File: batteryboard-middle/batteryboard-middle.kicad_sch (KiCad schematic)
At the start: 10 parts, among them J1 Conn_01x02, J2 Conn_01x02, J3 FLE-110-01-G-DV-A, J4 FLE-110-01-G-DV-A, J5 FTS-110-01-L-DV-A, J6 FTS-110-01-L-DV-A

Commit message: Fixed Broken Merge
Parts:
- removed J3, J4: FLE-110-01-G-DV-A, mainboard:SAMTEC_FLE-110-01-G-DV-A, symbol Connector_Generic:Conn_02x10_Odd_Even
- removed J5, J6: FTS-110-01-L-DV-A, batteryboard:SAMTEC-FTS-110-01-X-DV-A, symbol Connector_Generic:Conn_02x10_Odd_Even
- added J1: FLE-105-01-G-DV-A, batteryboard:SAMTEC_FLE-105-01-G-DV-A, symbol Connector_Generic:Conn_02x05_Odd_Even
- added J4: FTS-105-01-L-DV-A, batteryboard:FTS-105-XX-YY-DV-A, symbol Connector_Generic:Conn_02x05_Odd_Even
- renumbered J1 to J3
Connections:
- net +3V3: now also J1.3 (Pin_3), J4.3 (Pin_3)
- net BATT_N_SW: now also J1.2 (Pin_2)
- net BATT_P: now also J1.9 (Pin_9), J4.9 (Pin_9)
- net BATT_P_SW: now also J1.1 (Pin_1)
- net GND: now also J1.4 (Pin_4), J4.4 (Pin_4)
- new net COIL_N: J1.8 (Pin_8), J4.8 (Pin_8)
- new net COIL_P: J1.7 (Pin_7), J4.7 (Pin_7)
- new net SCL3: J1.6 (Pin_6), J4.6 (Pin_6)
- new net SDA3: J1.5 (Pin_5), J4.5 (Pin_5)
- new net VBUS: J1.10 (Pin_10), J4.10 (Pin_10)
- no-connect marks 32 -> 2
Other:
- moved on the sheet: H1, H2, H3, H4, J2, J3

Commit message: Some changes
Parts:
- removed J1: FLE-105-01-G-DV-A, batteryboard:SAMTEC_FLE-105-01-G-DV-A, symbol Connector_Generic:Conn_02x05_Odd_Even
- removed J4: FTS-105-01-L-DV-A, batteryboard:FTS-105-XX-YY-DV-A, symbol Connector_Generic:Conn_02x05_Odd_Even
- added J1: FLE-107-01-G-DV-A, batteryboard:SAMTEC_FLE-107-01-G-DV-A, symbol Connector_Generic:Conn_02x07_Odd_Even
- added J4: FTS-107-01-L-DV-A, batteryboard:SAMTEC-FTS-107-01-X-DV-A, symbol Connector_Generic:Conn_02x07_Odd_Even
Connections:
- net +3V3: now also J1.3 (Pin_3), J1.5 (Pin_5), J4.3 (Pin_3), J4.5 (Pin_5)
- net BATT_N_SW: now also J1.10 (Pin_10), J1.8 (Pin_8), J4.10 (Pin_10), J4.8 (Pin_8)
- net BATT_P: now also J1.7 (Pin_7), J1.9 (Pin_9), J4.7 (Pin_7), J4.9 (Pin_9)
- net BATT_P_SW: now also J1.4 (Pin_4), J1.6 (Pin_6), J4.4 (Pin_4), J4.6 (Pin_6)
- net GND: now also J1.1 (Pin_1), J1.2 (Pin_2), J4.1 (Pin_1), J4.2 (Pin_2)
- new net COIL5_N: J1.14 (Pin_14), J4.14 (Pin_14)
- new net COIL5_P: J1.12 (Pin_12), J4.12 (Pin_12)
- new net SCL1: J1.11 (Pin_11), J4.11 (Pin_11)
- new net SDA1: J1.13 (Pin_13), J4.13 (Pin_13)
- no-connect marks 2 -> 0
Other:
- note added: "Stack Conn - From Bottom Batteryboard"
- note added: "Stack Conn - To Top Batteryboard"
- note removed: "Stack Conn - From Batteryboard Bottom"
- note removed: "Stack Conn - To Batteryboard Top"
- moved on the sheet: H1, H2, H3, H4

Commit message: B2/01 Updates
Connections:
- net +3V3: now also J1.7 (Pin_7), J4.7 (Pin_7); no longer J1.3 (Pin_3), J4.3 (Pin_3)
- net BATT_N_SW: now also J1.2 (Pin_2), J1.4 (Pin_4), J4.2 (Pin_2), J4.4 (Pin_4); no longer J1.10 (Pin_10), J1.8 (Pin_8), J4.10 (Pin_10), J4.8 (Pin_8)
- net BATT_P: now also J1.10 (Pin_10), J1.12 (Pin_12), J4.10 (Pin_10), J4.12 (Pin_12); no longer J1.7 (Pin_7), J1.9 (Pin_9), J4.7 (Pin_7), J4.9 (Pin_9)
- net BATT_P_SW: now also J1.8 (Pin_8), J4.8 (Pin_8); no longer J1.4 (Pin_4), J4.4 (Pin_4)
- net COIL5_P: now also J1.13 (Pin_13), J4.13 (Pin_13); no longer J1.12 (Pin_12), J4.12 (Pin_12)
- net GND: now also J1.3 (Pin_3), J4.3 (Pin_3); no longer J1.2 (Pin_2), J4.2 (Pin_2)
- net SCL1: now also J1.9 (Pin_9), J4.9 (Pin_9); no longer J1.11 (Pin_11), J4.11 (Pin_11)
- net SDA1: now also J1.11 (Pin_11), J4.11 (Pin_11); no longer J1.13 (Pin_13), J4.13 (Pin_13)
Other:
- moved on the sheet: J1

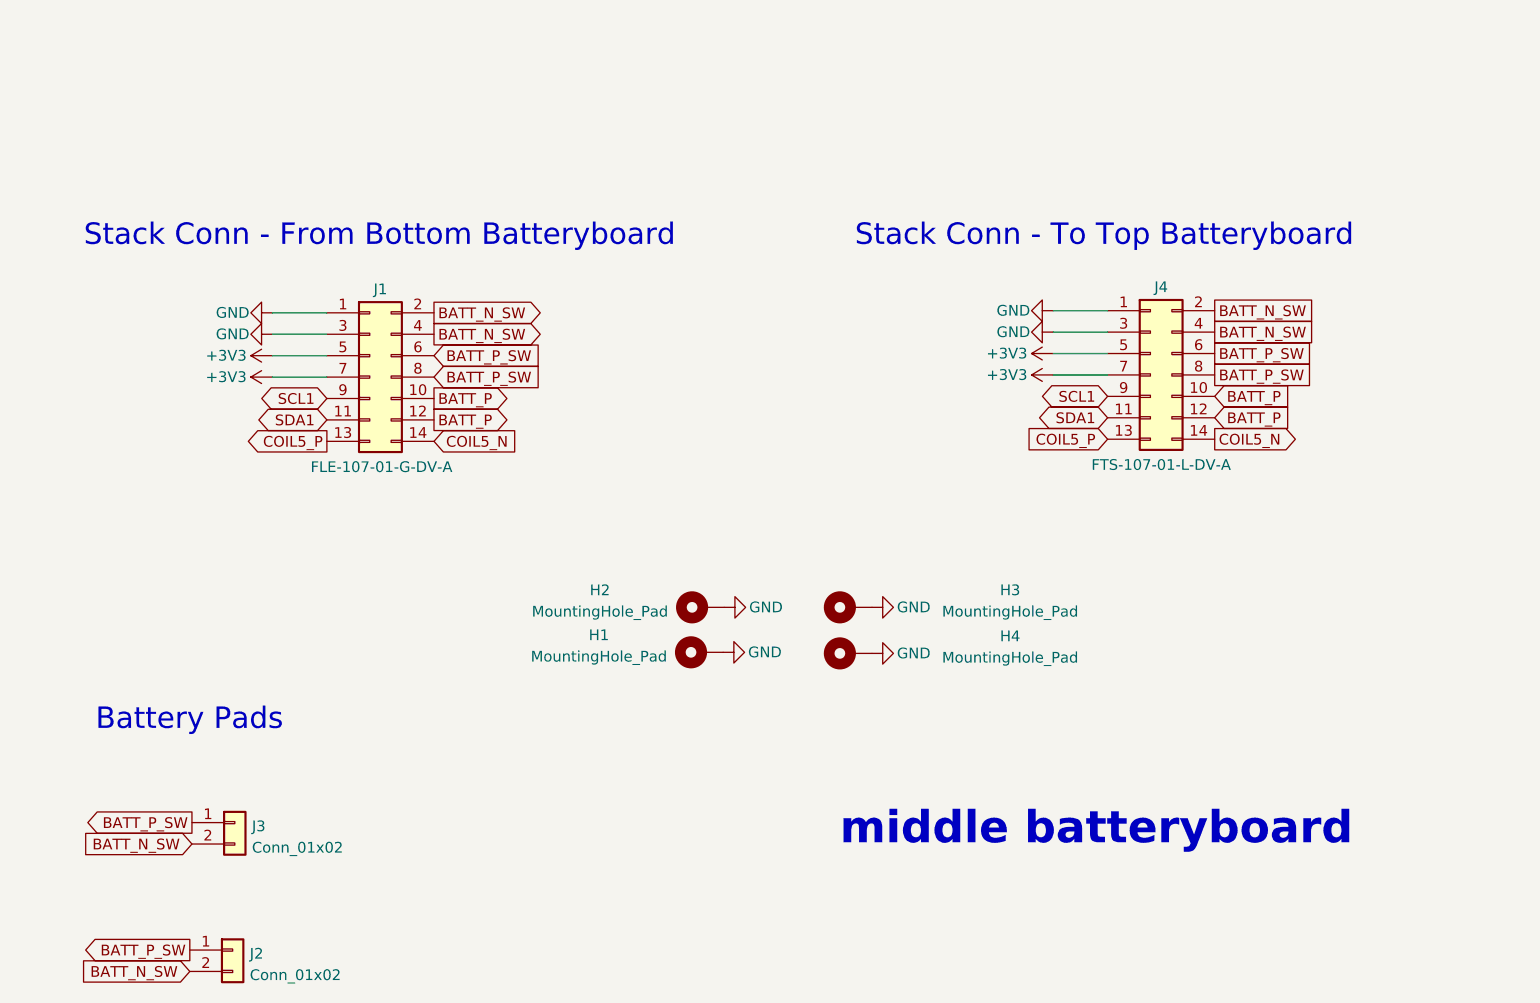
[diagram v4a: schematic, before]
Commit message: Updated batteryboards for Rev B3/01
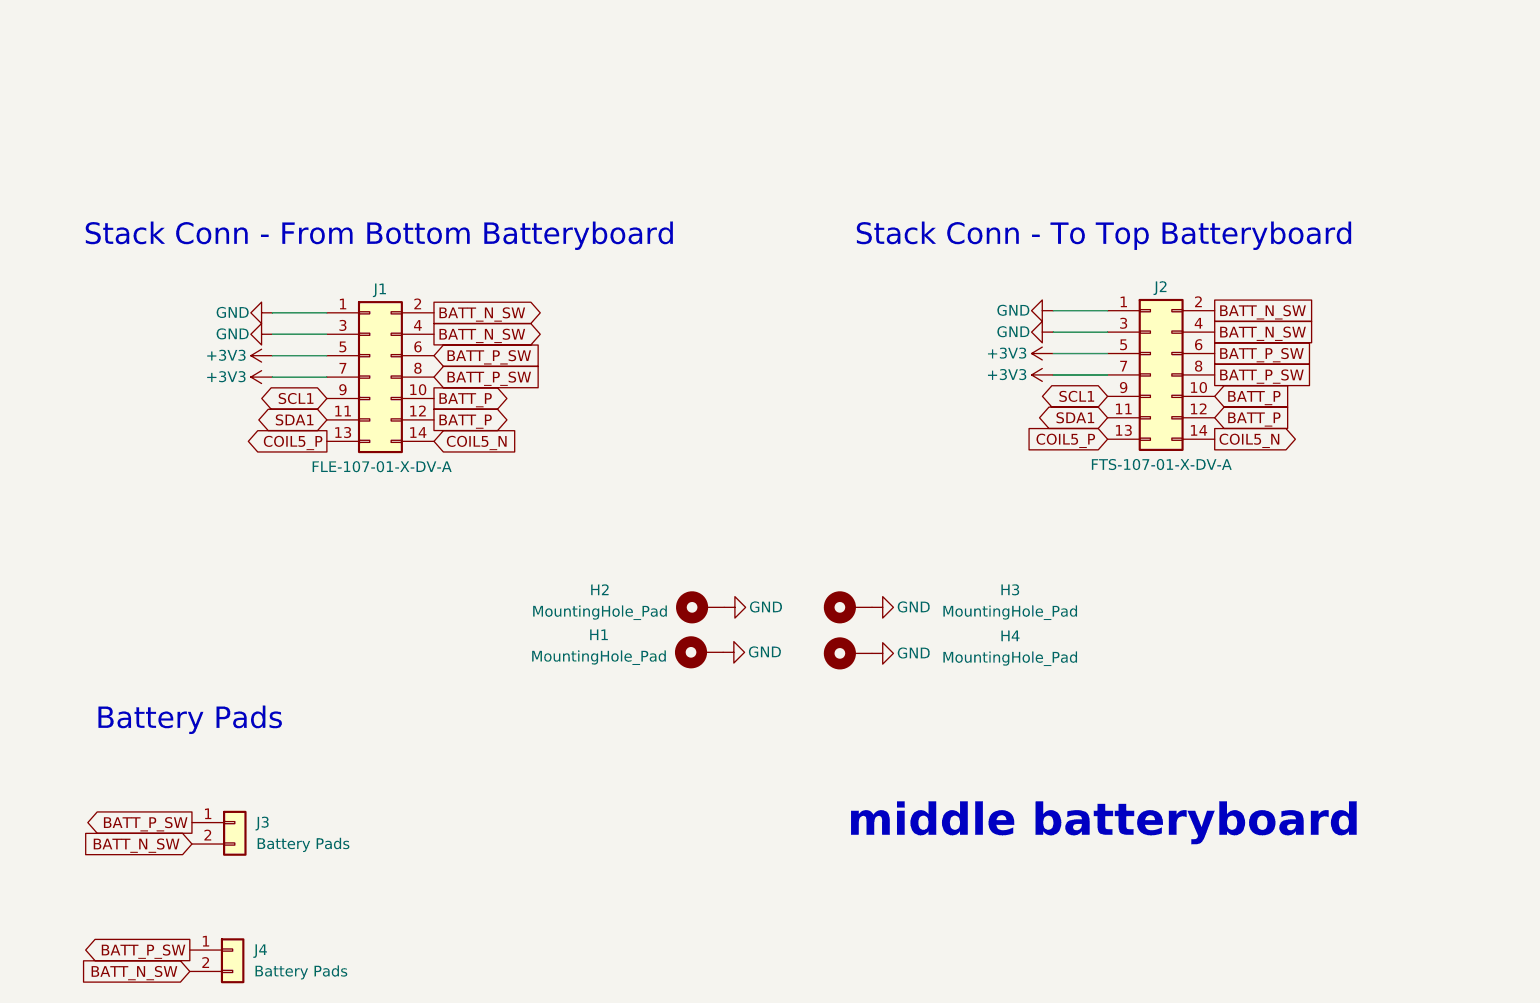
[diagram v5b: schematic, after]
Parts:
- J1: value FLE-107-01-G-DV-A -> FLE-107-01-X-DV-A; footprint batteryboard:SAMTEC_FLE-107-01-G-DV-A -> batteryboard:SAMTEC_FLE-107-01-X-DV-A
- J2: renamed from J4; value FTS-107-01-L-DV-A -> FTS-107-01-X-DV-A
- J3: value Conn_01x02 -> Battery Pads
- J4: renamed from J2; value Conn_01x02 -> Battery Pads

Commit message: Updated BOMs and STEP files
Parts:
- H1, H2, H3, H4, J3, J4: now left out of the parts list
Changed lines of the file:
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@@
   )
   (symbol (lib_id "Mechanical:MountingHole_Pad") (at 98.552 91.567 90) (unit 1)
-    (in_bom yes) (on_board yes) (dnp no)
+    (in_bom no) (on_board yes) (dnp no)
     (property "Reference" "H1" (at 86.36 89.535 90)
       (effects (font (size 1.27 1.27)))
@@
   )
   (symbol (lib_id "Mechanical:MountingHole_Pad") (at 116.205 86.233 90) (unit 1)
-    (in_bom yes) (on_board yes) (dnp no)
+    (in_bom no) (on_board yes) (dnp no)
     (property "Reference" "H3" (at 135.128 84.201 90)
       (effects (font (size 1.27 1.27)))
@@
   )
   (symbol (lib_id "Mechanical:MountingHole_Pad") (at 116.205 91.694 90) (unit 1)
-    (in_bom yes) (on_board yes) (dnp no)
+    (in_bom no) (on_board yes) (dnp no)
     (property "Reference" "H4" (at 135.128 89.662 90)
       (effects (font (size 1.27 1.27)))
@@
   )
   (symbol (lib_id "Mechanical:MountingHole_Pad") (at 98.679 86.233 90) (unit 1)
-    (in_bom yes) (on_board yes) (dnp no)
+    (in_bom no) (on_board yes) (dnp no)
     (property "Reference" "H2" (at 86.487 84.2041 90)
       (effects (font (size 1.27 1.27)))
@@
   )
   (symbol (lib_id "Connector_Generic:Conn_01x02") (at 43.18 111.76 0) (unit 1)
-    (in_bom yes) (on_board yes) (dnp no)
+    (in_bom no) (on_board yes) (dnp no)
     (property "Reference" "J3" (at 45.72 111.76 0)
       (effects (font (size 1.27 1.27)) (justify left))
@@
   )
   (symbol (lib_id "Connector_Generic:Conn_01x02") (at 42.926 126.873 0) (unit 1)
-    (in_bom yes) (on_board yes) (dnp no)
+    (in_bom no) (on_board yes) (dnp no)
     (property "Reference" "J4" (at 45.466 126.873 0)
       (effects (font (size 1.27 1.27)) (justify left))
